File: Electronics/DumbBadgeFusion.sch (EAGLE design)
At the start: 149 parts, among them IC1 74245MTC, IC2 74245MTC, IC3 74245MTC, SW1 SPST_TACT-KMR2, T1 MMUN2133LT1G, U1 ATSAMD21J18A-AUT, U2 TPS61090RSAR, U3 MCP73871, U4 FAN5333BSX, U6 MAX3232, X4 32.768

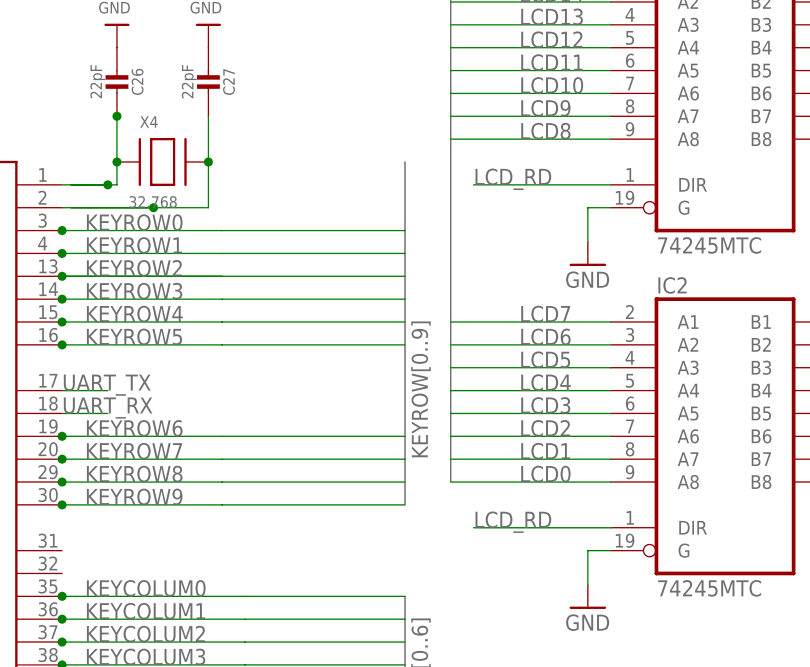
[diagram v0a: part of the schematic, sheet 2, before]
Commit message: almost done with keyboard
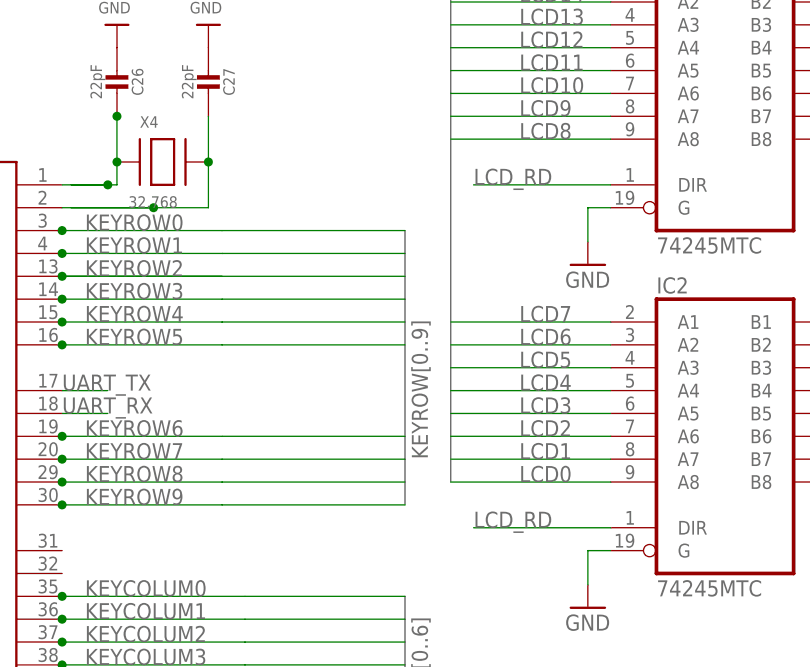
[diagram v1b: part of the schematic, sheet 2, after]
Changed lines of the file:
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@@
 <bus name="KEYROW[0..9]">
 <segment>
-<wire x1="137.16" y1="99.06" x2="137.16" y2="60.96" width="0.762" layer="92"/>
+<wire x1="137.16" y1="91.44" x2="137.16" y2="60.96" width="0.762" layer="92"/>
 <label x="139.7" y="66.04" size="1.778" layer="95" rot="R90"/>
 </segment>

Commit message: updated part names
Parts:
- X4: value 32.768 -> NX3215SA-32.768K-STD-MUA-8
- renumbered DIODES to TPD3E001, U$30 to FPC50CONN
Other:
- note removed: "+"
- note removed: "0"
- note removed: "1"
- note removed: "10"
- note removed: "11"
- note removed: "12"
- note removed: "13"
- note removed: "14"
- note removed: "15"
- note removed: "2"
- note removed: "3"
- note removed: "4"
- note removed: "5"
- note removed: "6"
- note removed: "7"
- note removed: "8"
- note removed: "9"
- note removed: "<"
- note removed: "?"
- note removed: "A"
- note removed: "B"
- note removed: "C"
- note removed: "Caps"
- note removed: "Control"
- note removed: "D"
- note removed: "F"
- note removed: "G"
- note removed: "H"
- note removed: "I"
- note removed: "J"
- note removed: "K"
- note removed: "L"
- note removed: "Left Alt"
- note removed: "Left Meta"
- note removed: "Line"
- note removed: "Lshift"
- note removed: "M"
- note removed: "N"
- note removed: "Noscl"
- note removed: "O"
- note removed: "P"
- note removed: "Pipe"
- note removed: "Right Meta"
- note removed: "RightAlt"
- note removed: "Row 0"
- note removed: "Row 1"
- note removed: "Row 2"
- note removed: "Row 3"
- note removed: "Row 4"
- note removed: "S"
- note removed: "Space"
- note removed: "U_score"
- note removed: "V"
- note removed: "X"
- note removed: "Z"
- note removed: "back"
- note removed: "break"
- note removed: "del"
- note removed: "down arrow"
- note removed: "e"
- note removed: "esc"
- note removed: "left arrow"
- note removed: "q"
- note removed: "quote"
- note removed: "r"
- note removed: "r shift"
- note removed: "return"
- note removed: "right arrow"
- note removed: "semi;"
- note removed: "setup"
- note removed: "t"
- note removed: "tab"
- note removed: "u"
- note removed: "up arrow"
- note removed: "w"
- note removed: "y"
- note removed: "{"
- note removed: "}"
- note removed: "~"

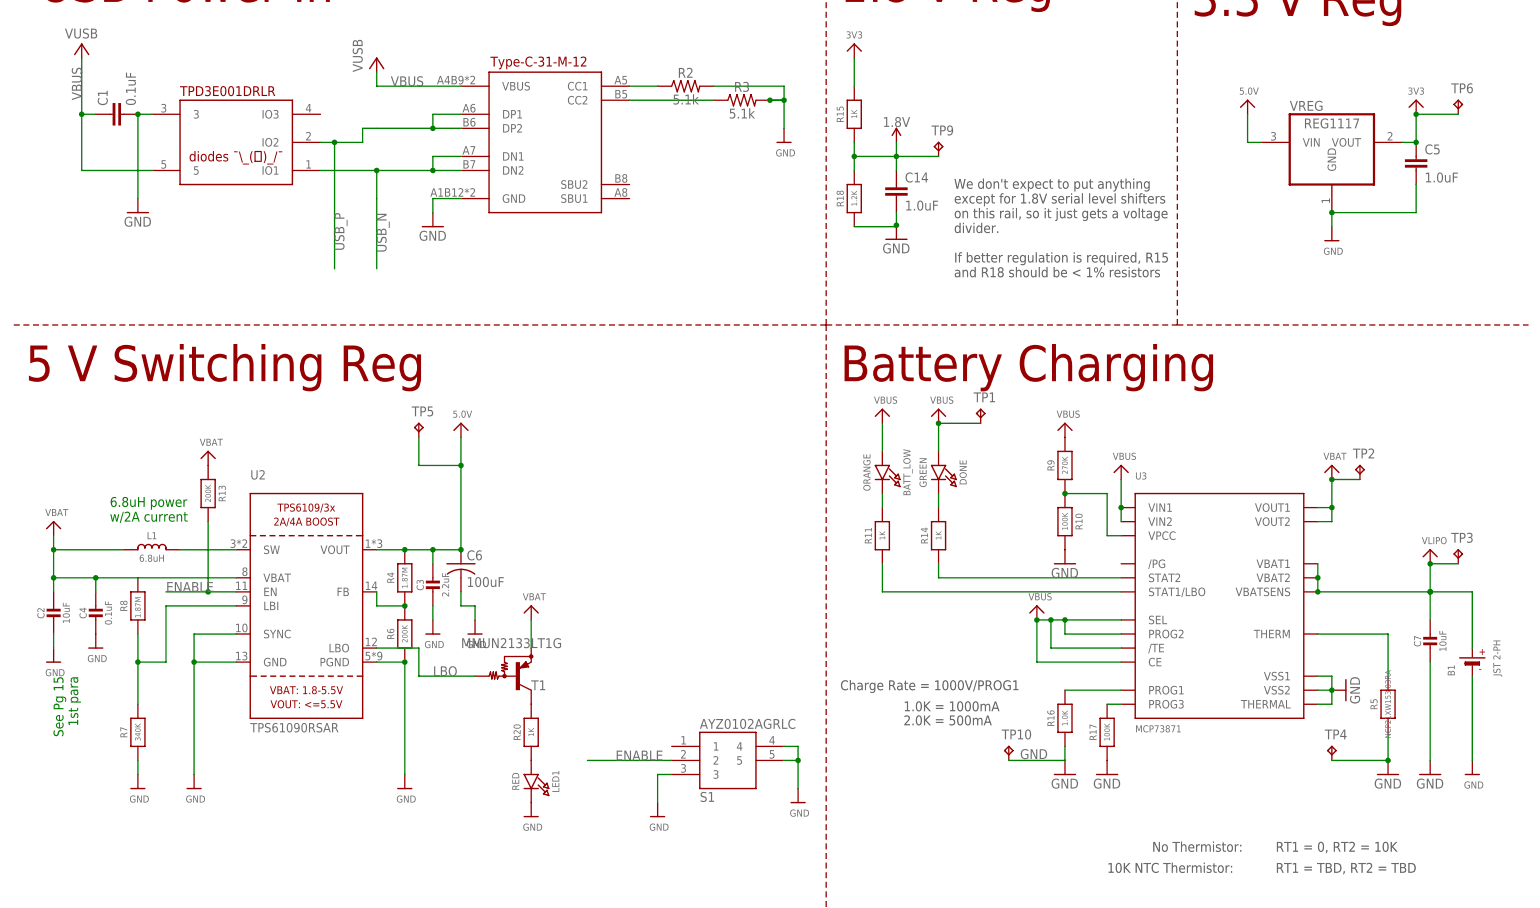
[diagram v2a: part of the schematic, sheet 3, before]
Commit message: Change to BOM, Macrofab order 2
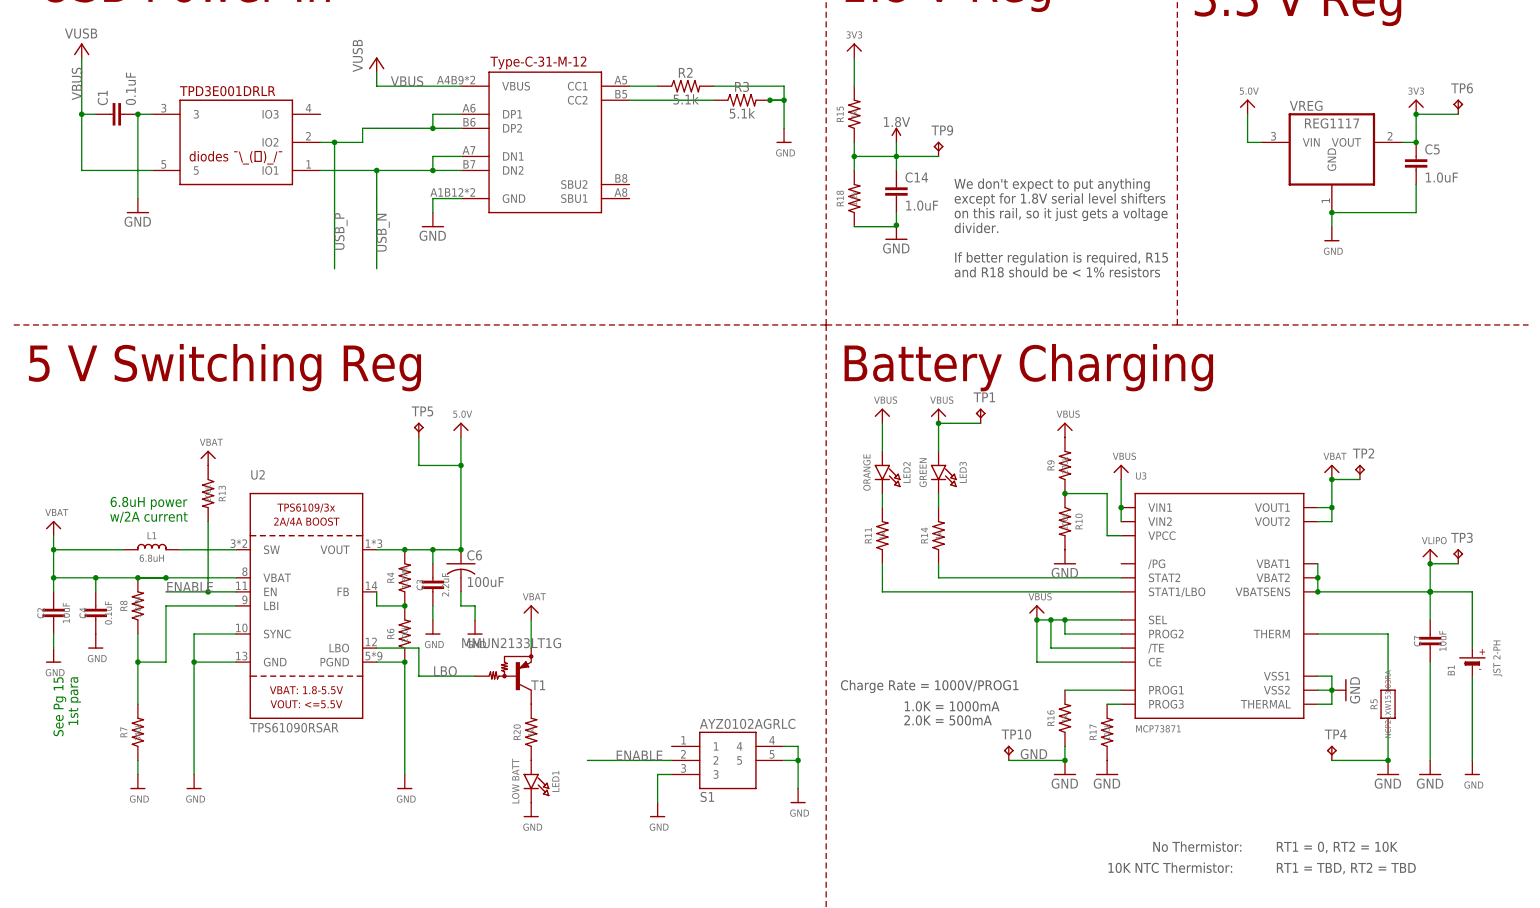
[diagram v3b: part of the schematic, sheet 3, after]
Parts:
- removed TP11: TPB1,27, testpad:TPB1,27
- C1: device SparkFun-Capacitors:1.0UF-0805-25V-(+80/-20%) -> SparkFun-Capacitors:1.0UF-0805-25V-10%
- C10, C11: value 1uF -> 1.0uF; device SparkFun-Capacitors:0.1UF-0603-25V-(+80/-20%) -> SparkFun-Capacitors:1.0UF-0805-25V-10%
- C14, C5: device SparkFun-Capacitors:1.0UF-0603-16V-10% -> SparkFun-Capacitors:1.0UF-0805-25V-10%
- C2, C3, C7: device microbuilder:CAP_CERAMIC0805-NOOUTLINE -> SparkFun-Capacitors:1.0UF-0805-25V-10%
- C22, C23, C24, C26, C27: device microbuilder:CAP_CERAMIC0603_NO -> SparkFun-Capacitors:1.0UF-0805-25V-10%
- C4: device microbuilder:CAP_CERAMIC0805_10MGAP -> SparkFun-Capacitors:1.0UF-0805-25V-10%
- C8, C9: device SparkFun-Capacitors:0.1UF-0603-25V-(+80/-20%) -> SparkFun-Capacitors:1.0UF-0805-25V-10%
- LED1: value RED -> LOW BATT
- R1: device adafruit:R-US_R0603 -> SparkFun-Resistors:1KOHM-0603-1/10W-1%
- R10, R17: value 100K -> 100k; device microbuilder:RESISTOR0805_NOOUTLINE -> SparkFun-Resistors:1KOHM-0603-1/10W-1%
- R11, R14, R15, R20: value 1K -> 1k; device microbuilder:RESISTOR0805_NOOUTLINE -> SparkFun-Resistors:1KOHM-0603-1/10W-1%
- R12: value 6Ω -> 6 Ohm; device adafruit:R-US_R0603 -> SparkFun-Resistors:1KOHM-0603-1/10W-1%
- R13, R6: value 200K -> 200k; device microbuilder:RESISTOR0805_NOOUTLINE -> SparkFun-Resistors:1KOHM-0603-1/10W-1%
- R16: value 1.0K -> 1k; device microbuilder:RESISTOR0805_NOOUTLINE -> SparkFun-Resistors:1KOHM-0603-1/10W-1%
- R18: value 1.2K -> 1.2k; device microbuilder:RESISTOR0805_NOOUTLINE -> SparkFun-Resistors:1KOHM-0603-1/10W-1%
- R19: value 0 -> 0 Ohm; device SparkFun-Resistors:5.62KOHM-0603-1/10W-1% -> SparkFun-Resistors:1KOHM-0603-1/10W-1%
- R2, R3: device SparkFun-Resistors:5.62KOHM-0603-1/10W-1% -> SparkFun-Resistors:1KOHM-0603-1/10W-1%
- R4: device microbuilder:RESISTOR0805_NOOUTLINE -> SparkFun-Resistors:1KOHM-0603-1/10W-1%
- R7: value 340K -> 340k; device microbuilder:RESISTOR_0805MP -> SparkFun-Resistors:1KOHM-0603-1/10W-1%
- R8: device microbuilder:RESISTOR_0805MP -> SparkFun-Resistors:1KOHM-0603-1/10W-1%
- R9: value 270K -> 270k; device microbuilder:RESISTOR0805_NOOUTLINE -> SparkFun-Resistors:1KOHM-0603-1/10W-1%
- renumbered BATT_LOW to LED2, DONE to LED3
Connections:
- net KEYROW6: now also K_BACK.P$1

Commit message: more stuff
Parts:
- renumbered TPD3E001 to U5
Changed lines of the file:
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@@
 <part name="R3" library="SparkFun-Resistors" library_urn="urn:adsk.eagle:library:532" deviceset="1KOHM" device="-0603-1/10W-1%" package3d_urn="urn:adsk.eagle:package:39650/1" value="5.1k"/>
 <part name="U$6" library="microbuilder" deviceset="GND" device=""/>
-<part name="TPD3E001" library="USBC" deviceset="TDP3E001DRLR-SOT-23-5" device="SOT-23-5"/>
+<part name="U5" library="USBC" deviceset="TDP3E001DRLR-SOT-23-5" device="SOT-23-5"/>
 <part name="P+1" library="supply1" library_urn="urn:adsk.eagle:library:371" deviceset="VCC" device="" value="VUSB"/>
 <part name="P+2" library="supply1" library_urn="urn:adsk.eagle:library:371" deviceset="VCC" device="" value="VUSB"/>
@@
 <attribute name="VALUE" x="140.716" y="218.44" size="1.27" layer="96"/>
 </instance>
-<instance part="TPD3E001" gate="G$1" x="40.64" y="220.98" smashed="yes" rot="R180"/>
+<instance part="U5" gate="G$1" x="40.64" y="220.98" smashed="yes" rot="R180"/>
 <instance part="P+1" gate="VCC" x="68.58" y="236.22" smashed="yes">
 <attribute name="VALUE" x="66.04" y="233.68" size="1.778" layer="96" rot="R90"/>
@@
 </segment>
 <segment>
-<pinref part="TPD3E001" gate="G$1" pin="3"/>
+<pinref part="U5" gate="G$1" pin="3"/>
 <pinref part="C1" gate="G$1" pin="2"/>
 <wire x1="27.94" y1="226.06" x2="25.4" y2="226.06" width="0.1524" layer="91"/>
@@
 <wire x1="78.74" y1="215.9" x2="68.58" y2="215.9" width="0.1524" layer="91"/>
 <junction x="78.74" y="215.9"/>
-<pinref part="TPD3E001" gate="G$1" pin="IO1"/>
+<pinref part="U5" gate="G$1" pin="IO1"/>
 <wire x1="68.58" y1="215.9" x2="58.42" y2="215.9" width="0.1524" layer="91"/>
 <wire x1="68.58" y1="210.82" x2="68.58" y2="215.9" width="0.1524" layer="91"/>
@@
 <wire x1="68.58" y1="223.52" x2="66.04" y2="223.52" width="0.1524" layer="91"/>
 <wire x1="66.04" y1="223.52" x2="66.04" y2="220.98" width="0.1524" layer="91"/>
-<pinref part="TPD3E001" gate="G$1" pin="IO2"/>
+<pinref part="U5" gate="G$1" pin="IO2"/>
 <wire x1="66.04" y1="220.98" x2="60.96" y2="220.98" width="0.1524" layer="91"/>
 <wire x1="60.96" y1="220.98" x2="58.42" y2="220.98" width="0.1524" layer="91"/>
@@
 <wire x1="15.24" y1="236.22" x2="15.24" y2="233.68" width="0.1524" layer="91"/>
 <wire x1="15.24" y1="233.68" x2="15.24" y2="226.06" width="0.1524" layer="91"/>
-<pinref part="TPD3E001" gate="G$1" pin="5"/>
+<pinref part="U5" gate="G$1" pin="5"/>
 <wire x1="15.24" y1="226.06" x2="15.24" y2="215.9" width="0.1524" layer="91"/>
 <wire x1="15.24" y1="215.9" x2="27.94" y2="215.9" width="0.1524" layer="91"/>

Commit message: created keyboard standalone, improved schematics
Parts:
- removed U$32: RPI-ZERO, RPI-Zero:RPI-ZERO
- added U$30: SAMTEC_PI_REVERSE, FPC:SAMTEC_PI_REVERSE
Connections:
- net 5.0V: now also U$30.P2, U$30.P4; no longer U$32.5V0@1, U$32.5V0@2
- net GND: now also U$30.P14, U$30.P25, U$30.P30, U$30.P34, U$30.P39, U$30.P6, U$30.P9; no longer U$32.GND@1, U$32.GND@2, U$32.GND@3, U$32.GND@4, U$32.GND@5, U$32.GND@6, U$32.GND@7, U$32.GND@8
- net PB31: now also U$30.P1; no longer U$32.3V3@1
- net UART_RX: now also U$30.P10; no longer U$32.RXD0/GPIO15
- net UART_TX: now also U$30.P8; no longer U$32.TXD0/GPIO14
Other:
- note added: "Raspberry Pi Zero Adapter"
- note removed: "10K NTC Thermistor:"
- note removed: "No Thermistor:"
- note removed: "RT1 = 0, RT2 = 10K"
- note removed: "RT1 = TBD, RT2 = TBD"
